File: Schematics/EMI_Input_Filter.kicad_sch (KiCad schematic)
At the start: 3 parts

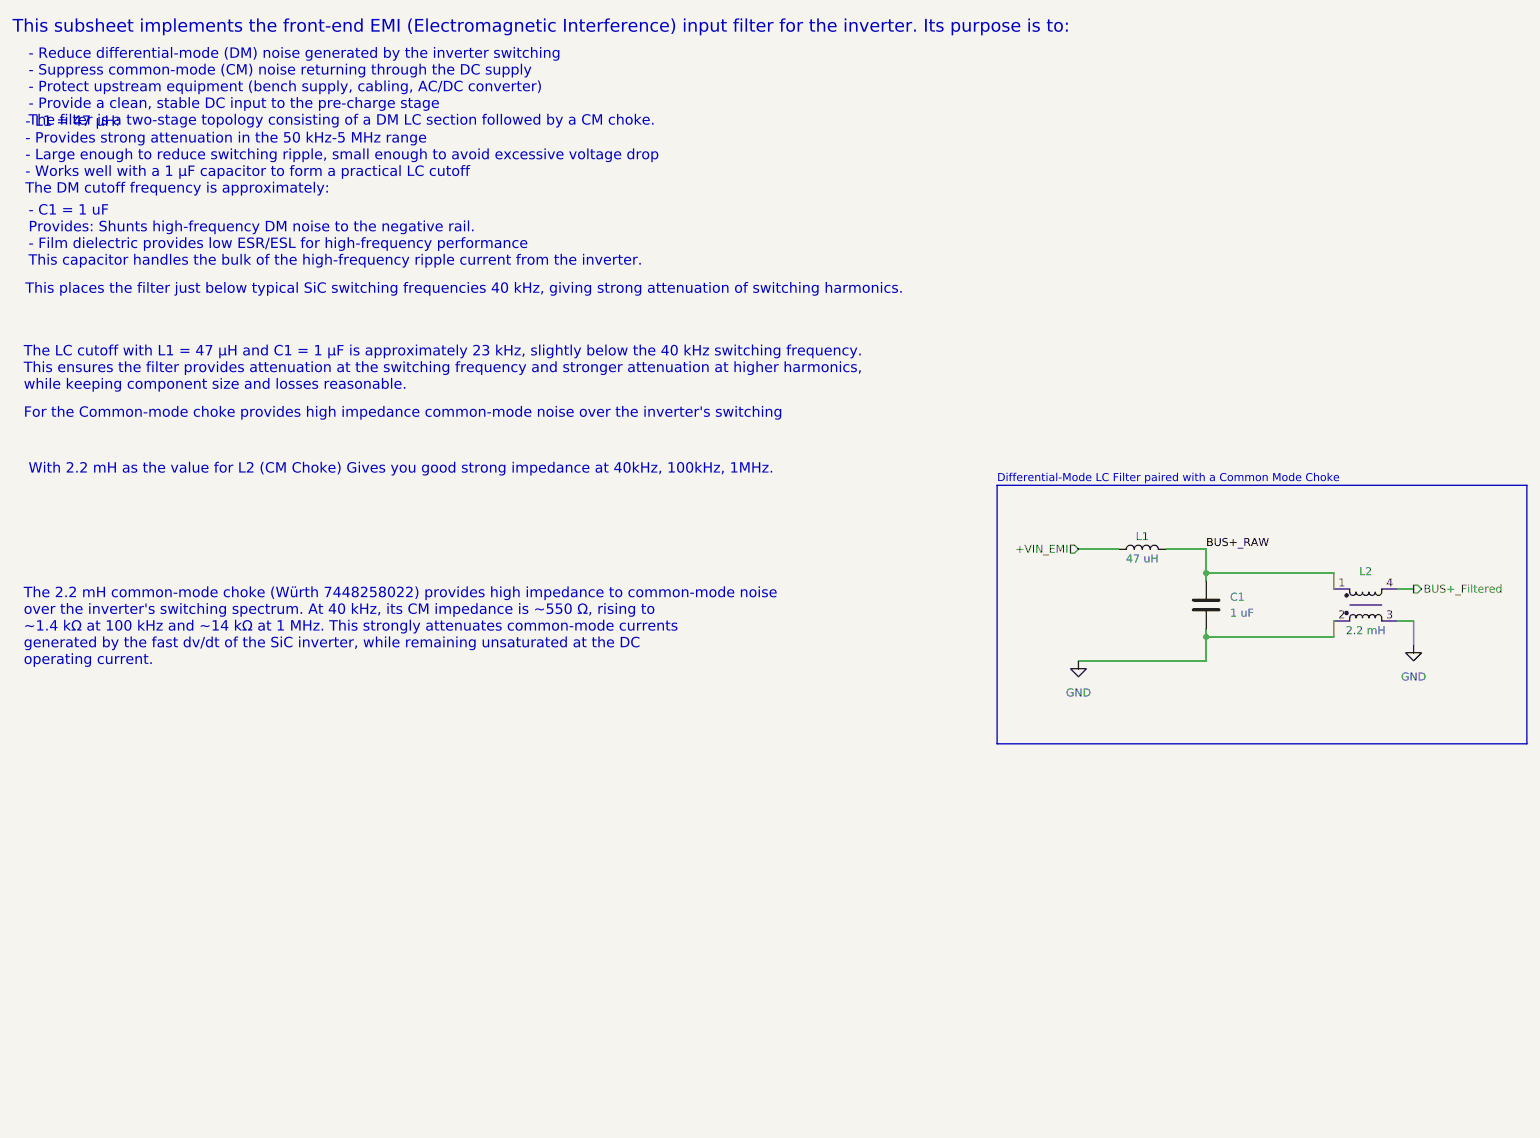
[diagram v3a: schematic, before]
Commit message: [WIP SiC Single Phase Inverter]
- Added PCB to PCB Male and Female connectors
- Added symbols, footprints and 3d models for the parts listed above
- Added Male and Female connectors to input protection and input emi
  subsheets
- Changed PCB editor to account for two edge cuts/ two sub circuits
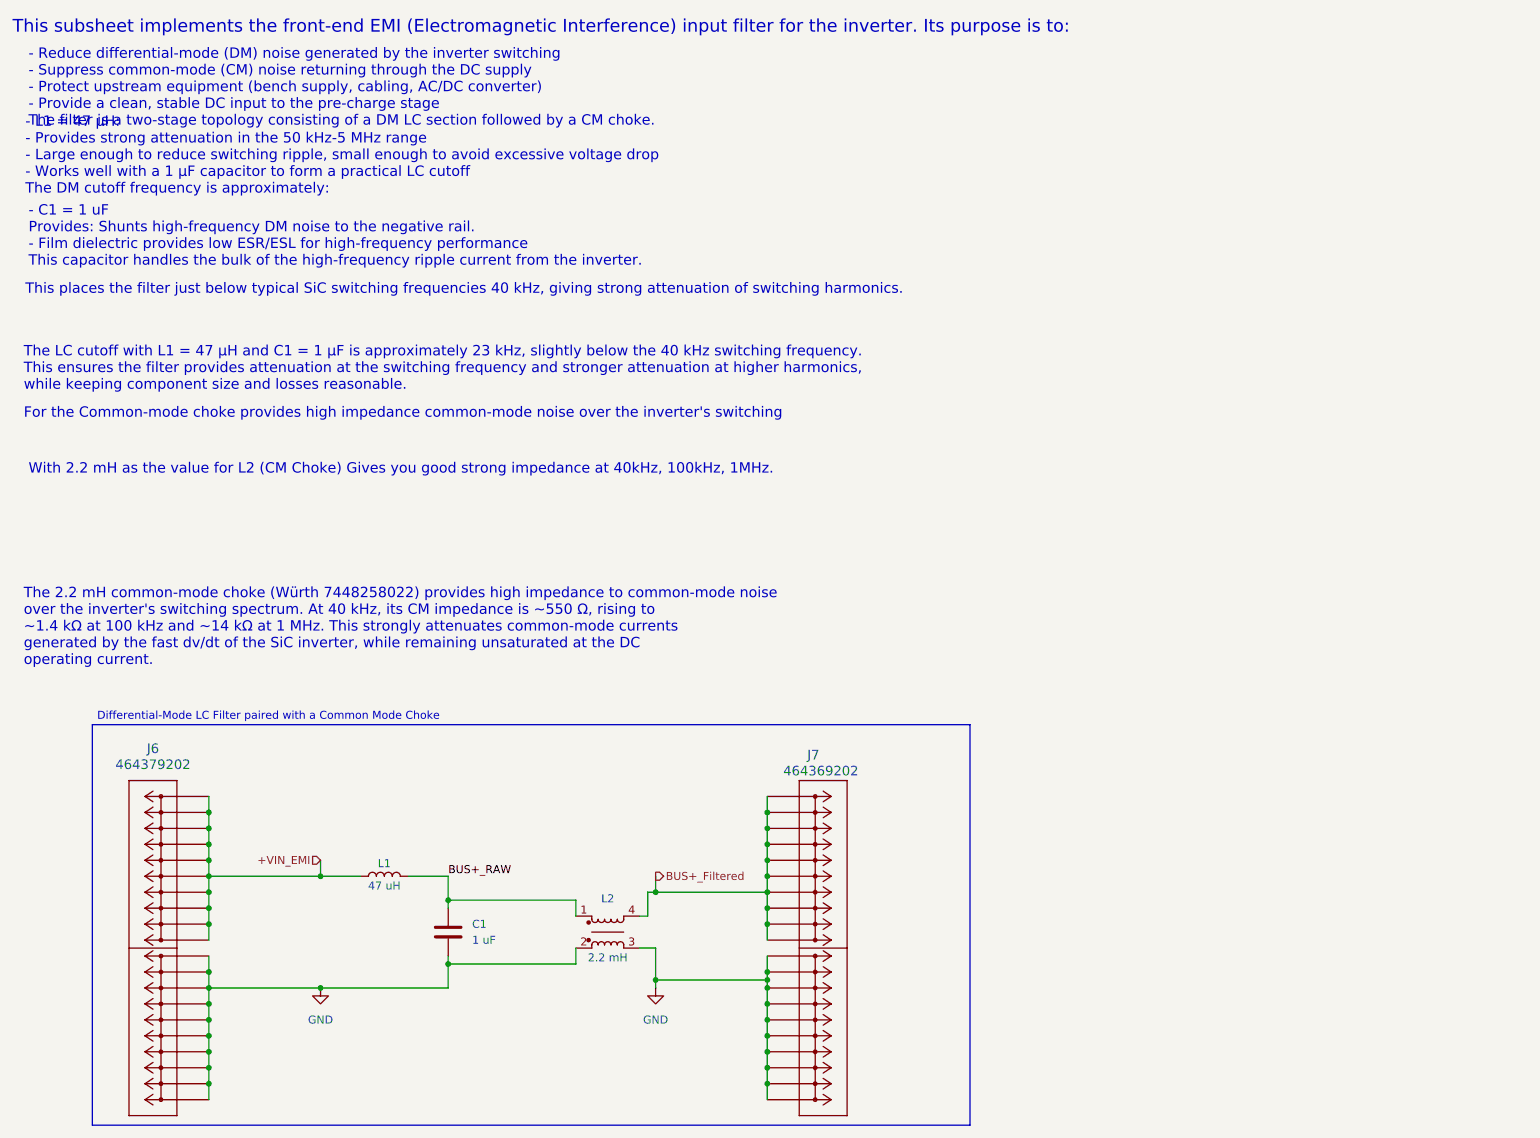
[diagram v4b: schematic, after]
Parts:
- added J6: 464379202, SiC_Inverter:46437-900_02, symbol SiC_Inverter:464379202
- added J7: 464369202, SiC_Inverter:46436-900_02, symbol SiC_Inverter:464369202
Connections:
- net +VIN_EMI: now also J6.P2_1, J6.P2_10, J6.P2_2, J6.P2_3, J6.P2_4, J6.P2_5, J6.P2_6, J6.P2_7, J6.P2_8, J6.P2_9
- net BUS+_Filtered: now also J7.P1_1, J7.P1_10, J7.P1_2, J7.P1_3, J7.P1_4, J7.P1_5, J7.P1_6, J7.P1_7, J7.P1_8, J7.P1_9
- net GND: now also J6.P1_1, J6.P1_10, J6.P1_2, J6.P1_3, J6.P1_4, J6.P1_5, J6.P1_6, J6.P1_7, J6.P1_8, J6.P1_9, J7.P2_1, J7.P2_10, J7.P2_2, J7.P2_3, J7.P2_4, J7.P2_5, J7.P2_6, J7.P2_7, J7.P2_8, J7.P2_9
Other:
- moved on the sheet: C1, L1, L2

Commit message: Changing Text to Text Block
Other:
- note removed: "Differential-Mode LC Filter paired with a Common Mode Choke"
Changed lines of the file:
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@@
-		)
-	)
-	(text "Differential-Mode LC Filter paired with a Common Mode Choke"
-		(exclude_from_sim no)
-		(at 26.67 125.73 0)
-		(effects
-			(font
-				(size 1.27 1.27)
-			)
-			(justify left)
 		)
 	)
@@
 		)
 	)
+	(text_box "Differential-Mode LC Filter paired with a Common Mode Choke"
+		(exclude_from_sim no)
+		(at 25.908 123.698 0)
+		(size 64.008 3.048)
+		(margins 0.9525 0.9525 0.9525 0.9525)
+		(stroke
+			(width 0)
+			(type solid)
+		)
+		(fill
+			(type color)
+			(color 0 0 255 0.1)
+		)
+		(effects
+			(font
+				(size 1.27 1.27)
+			)
+			(justify left top)
+		)
+	)

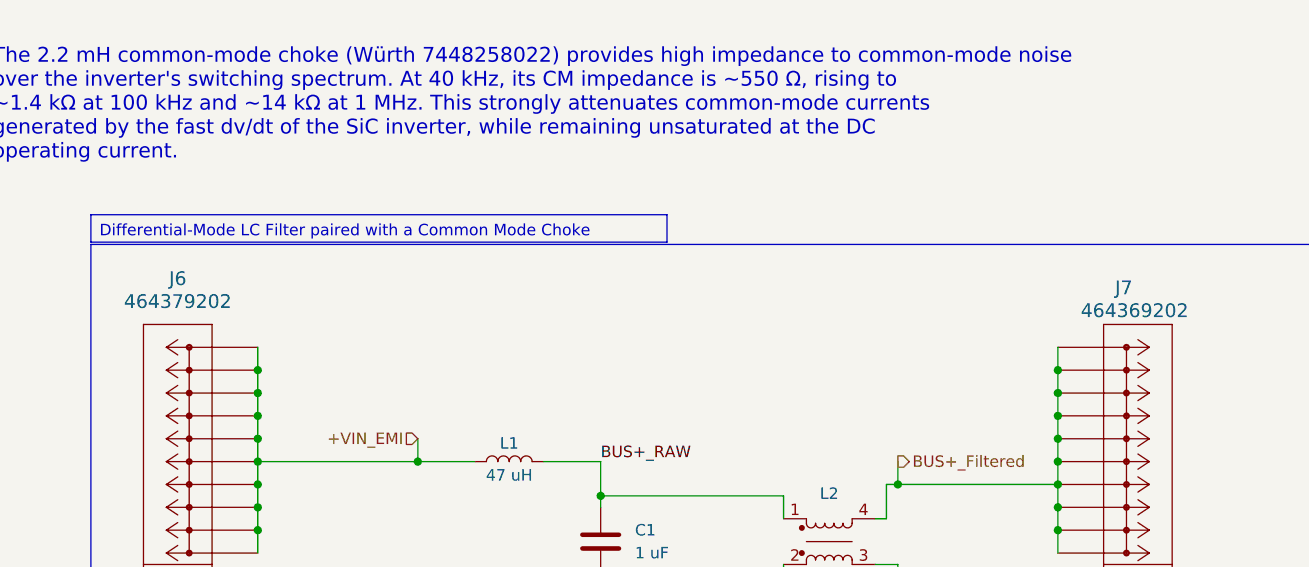
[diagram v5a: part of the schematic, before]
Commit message: [WIP Single Phase Inverter]
- Changed all Refs within each sub sheet (Stripe)
- Added 3V3 Power Supply off of 15V iso supply
- Added footprint, symbol and 3d part
- updated PCB with new part
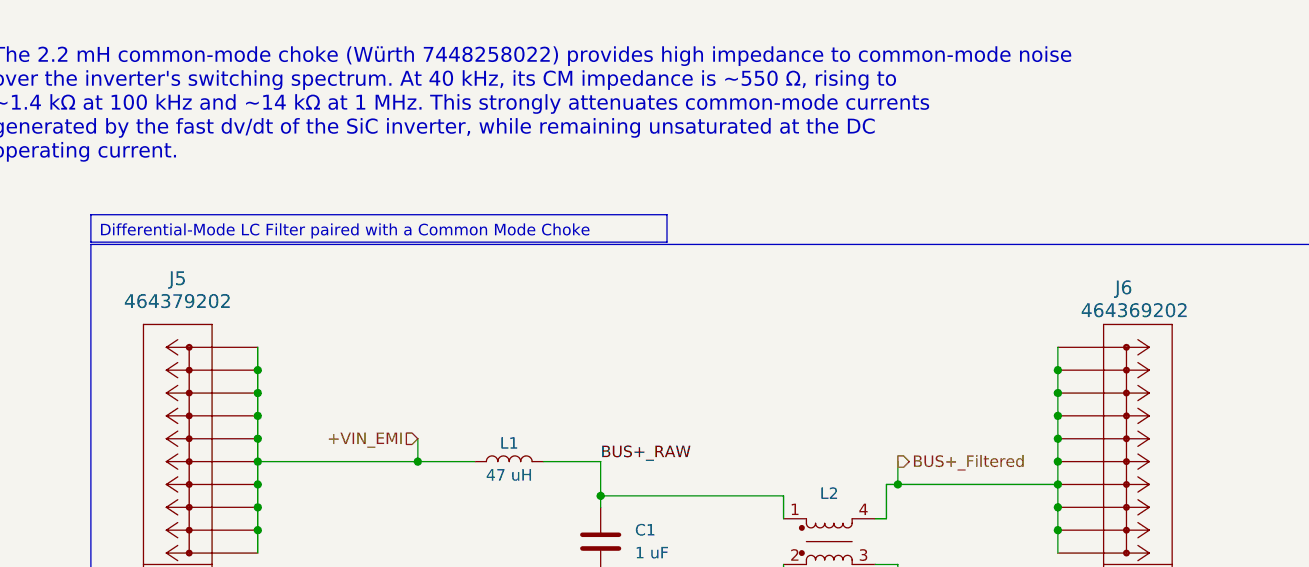
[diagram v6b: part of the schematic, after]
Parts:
- renumbered J6 to J5, J7 to J6
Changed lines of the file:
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@@
 		(dnp no)
 		(fields_autoplaced yes)
-		(property "Reference" "J6"
+		(property "Reference" "J5"
 			(at 35.56 130.81 0)
 			(effects
@@
 			(project ""
 				(path "/a1ed0539-9735-4ad1-a8fd-87e26e7fce16/7998be36-55a1-424f-a315-c3fdbc8a6aca"
-					(reference "J6")
+					(reference "J5")
 					(unit 1)
 				)
@@
 		(on_board yes)
 		(dnp no)
-		(property "Reference" "J7"
+		(property "Reference" "J6"
 			(at 139.7 131.826 0)
 			(effects
@@
 			(project "SiC_Single_Phase_Inverter"
 				(path "/a1ed0539-9735-4ad1-a8fd-87e26e7fce16/7998be36-55a1-424f-a315-c3fdbc8a6aca"
-					(reference "J7")
+					(reference "J6")
 					(unit 1)
 				)
@@
 		(dnp no)
 		(fields_autoplaced yes)
-		(property "Reference" "#PWR07"
+		(property "Reference" "#PWR04"
 			(at 115.57 175.26 0)
 			(effects
@@
 			(project "SiC_Single_Phase_Inverter"
 				(path "/a1ed0539-9735-4ad1-a8fd-87e26e7fce16/7998be36-55a1-424f-a315-c3fdbc8a6aca"
-					(reference "#PWR07")
+					(reference "#PWR04")
 					(unit 1)
 				)
@@
 		(dnp no)
 		(fields_autoplaced yes)
-		(property "Reference" "#PWR04"
+		(property "Reference" "#PWR03"
 			(at 62.23 175.26 0)
 			(effects
@@
 			(project "SiC_Single_Phase_Inverter"
 				(path "/a1ed0539-9735-4ad1-a8fd-87e26e7fce16/7998be36-55a1-424f-a315-c3fdbc8a6aca"
-					(reference "#PWR04")
-					(unit 1)
-				)
+					(reference "#PWR03")
+					(unit 1)
+				)

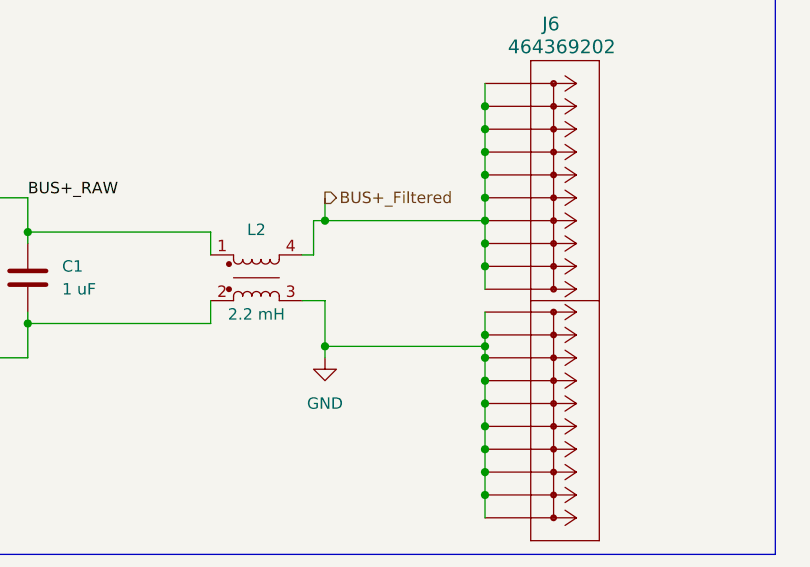
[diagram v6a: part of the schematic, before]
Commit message: [Milestone Compelted Controller and USB]
- Added Test Points
- Completed USB circuit to Controller
- Wired up Controller
- Added Connectors to Power Subsheet and 12pin from cotnroller to Full
  Bridge
- Added 3d models for USB compoents
- General fixes to subsheets
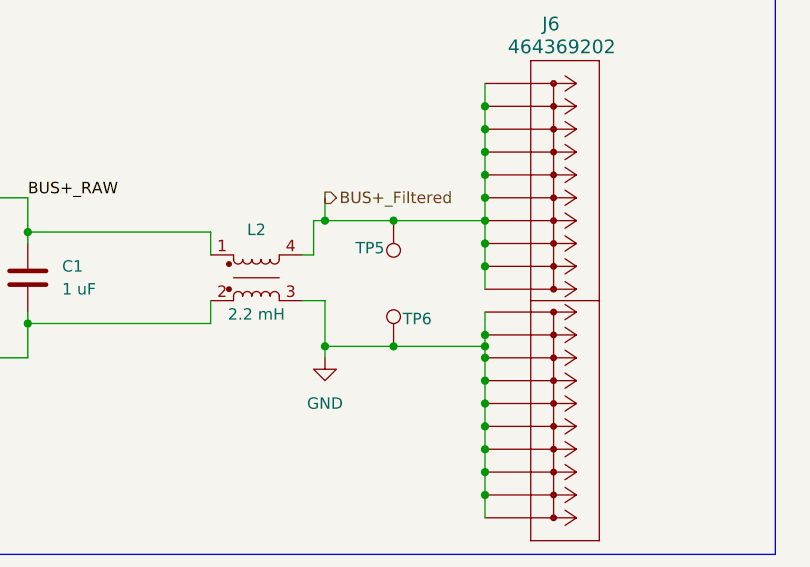
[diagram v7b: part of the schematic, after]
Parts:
- added TP5: 5277, SiC_Inverter:5277, symbol SiC_Inverter:5277
- added TP6: 5281, SiC_Inverter:5281, symbol SiC_Inverter:5281
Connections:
- net BUS+_Filtered: now also TP5.1
- net GND: now also TP6.1
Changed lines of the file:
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@@
+	)
+	(junction
+		(at 123.19 167.64)
+		(diameter 0)
+		(color 0 0 0 0)
 	)
 	(junction
@@
 	)
 	(junction
+		(at 123.19 153.67)
+		(diameter 0)
+		(color 0 0 0 0)
+	)
+	(junction
 		(at 133.35 171.45)
 		(diameter 0)
@@
 	(wire
 		(pts
-			(xy 115.57 153.67) (xy 133.35 153.67)
+			(xy 115.57 153.67) (xy 123.19 153.67)
 		)
 		(stroke
@@
 	(wire
 		(pts
+			(xy 123.19 153.67) (xy 133.35 153.67)
+		)
+		(stroke
+			(width 0)
+			(type default)
+		)
+	)
+	(wire
+		(pts
 			(xy 133.35 140.97) (xy 133.35 143.51)
 		)
@@
 	(wire
 		(pts
-			(xy 115.57 167.64) (xy 133.35 167.64)
+			(xy 115.57 167.64) (xy 123.19 167.64)
+		)
+		(stroke
+			(width 0)
+			(type default)
+		)
+	)
+	(wire
+		(pts
+			(xy 123.19 167.64) (xy 133.35 167.64)
 		)
 		(stroke
@@
 	)
 	(symbol
+		(lib_id "SiC_Inverter:5277")
+		(at 123.19 153.67 180)
+		(unit 1)
+		(exclude_from_sim no)
+		(in_bom yes)
+		(on_board yes)
+		(dnp no)
+		(property "Reference" "TP5"
+			(at 122.174 156.718 0)
+			(effects
+				(font
+					(size 1.27 1.27)
+				)
+				(justify left)
+			)
+		)
+		(property "Value" "5277"
+			(at 139.192 140.716 0)
+			(effects
+				(font
+					(size 1.27 1.27)
+				)
+				(hide yes)
+			)
+		)
+		(property "Footprint" "SiC_Inverter:5277"
+			(at 133.096 142.494 0)
+			(effects
+				(font
+					(size 1.27 1.27)
+				)
+				(hide yes)
+			)
+		)
+		(property "Datasheet" "https://www.keyelco.com/userAssets/file/K75p62.pdf"
+			(at 115.316 146.304 0)
+			(effects
+				(font
+					(size 1.27 1.27)
+				)
+				(hide yes)
+			)
+		)
+		(property "Description" "Test Plugs & Test Jacks TEST POINT (BLUE) - COMPACT"
+			(at 112.776 144.272 0)
+			(effects
+				(font
+					(size 1.27 1.27)
+				)
+				(hide yes)
+			)
+		)
+		(pin "1"
+		)
+		(instances
+			(project "SiC_Single_Phase_Inverter"
+				(path "/a1ed0539-9735-4ad1-a8fd-87e26e7fce16/7998be36-55a1-424f-a315-c3fdbc8a6aca"
+					(reference "TP5")
+					(unit 1)
+				)
+			)
+		)
+	)
+	(symbol
 		(lib_id "SiC_Inverter:464369202")
 		(at 133.35 138.43 0)
@@
 					(unit 1)
 				)
+			)
+		)
+	)
+	(symbol
+		(lib_id "SiC_Inverter:5281")
+		(at 123.19 167.64 0)
+		(unit 1)
+		(exclude_from_sim no)
+		(in_bom yes)
+		(on_board yes)
+		(dnp no)
+		(property "Reference" "TP6"
+			(at 124.206 164.592 0)
+			(effects
+				(font
+					(size 1.27 1.27)
+				)
+				(justify left)
+			)
+		)
+		(property "Value" "5281"
+			(at 107.188 180.594 0)
+			(effects
+				(font
+					(size 1.27 1.27)
+				)
+				(hide yes)
+			)
+		)
+		(property "Footprint" "SiC_Inverter:5281"
+			(at 113.284 178.816 0)
+			(effects
+				(font
+					(size 1.27 1.27)
+				)
+				(hide yes)
+			)
+		)
+		(property "Datasheet" "https://www.keyelco.com/userAssets/file/K75p62.pdf"
+			(at 131.064 175.006 0)
+			(effects
+				(font
+					(size 1.27 1.27)
+				)
+				(hide yes)
+			)
+		)
+		(property "Description" "Test Plugs & Test Jacks TEST POINT BLACK MULTIPURPOSE"
+			(at 133.604 177.038 0)
+			(effects
+				(font
+					(size 1.27 1.27)
+				)
+				(hide yes)
+			)
+		)
+		(pin "1"
+		)
+		(instances
+			(project "SiC_Single_Phase_Inverter"
+				(path "/a1ed0539-9735-4ad1-a8fd-87e26e7fce16/7998be36-55a1-424f-a315-c3fdbc8a6aca"
+					(reference "TP6")
+					(unit 1)
+				)

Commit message: WIP PCB, Added Test Points, added icon file
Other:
- moved on the sheet: TP5
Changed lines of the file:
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@@
 	(symbol
 		(lib_id "SiC_Inverter:5277")
-		(at 123.19 153.67 180)
+		(at 123.19 152.4 180)
 		(unit 1)
 		(exclude_from_sim no)
@@
 		(dnp no)
 		(property "Reference" "TP5"
-			(at 122.174 156.718 0)
+			(at 122.174 155.448 0)
 			(effects
 				(font
@@
 		)
 		(property "Value" "5277"
-			(at 139.192 140.716 0)
+			(at 139.192 139.446 0)
 			(effects
 				(font
@@
 		)
 		(property "Footprint" "SiC_Inverter:5277"
-			(at 133.096 142.494 0)
+			(at 133.096 141.224 0)
 			(effects
 				(font
@@
 		)
 		(property "Datasheet" "https://www.keyelco.com/userAssets/file/K75p62.pdf"
-			(at 115.316 146.304 0)
+			(at 115.316 145.034 0)
 			(effects
 				(font
@@
 		)
 		(property "Description" "Test Plugs & Test Jacks TEST POINT (BLUE) - COMPACT"
-			(at 112.776 144.272 0)
+			(at 112.776 143.002 0)
 			(effects
 				(font
